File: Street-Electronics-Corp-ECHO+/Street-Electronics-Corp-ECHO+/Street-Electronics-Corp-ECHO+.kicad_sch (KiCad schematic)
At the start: 57 parts, among them J1 Bus_Apple_II_Card_Side, J2 STEREO, J3 MONO, U1 LM386, U10 74C74, U11 74LS02, U12 74LS02, U13 74LS02, U14 74LS02, U15 74LS00, U2 LM386, U3 TL084, U4 AY-3-8913, U5 AY-3-8913, U6 6522, U7 TMS5220, U8 74LS373, U9 74SC373

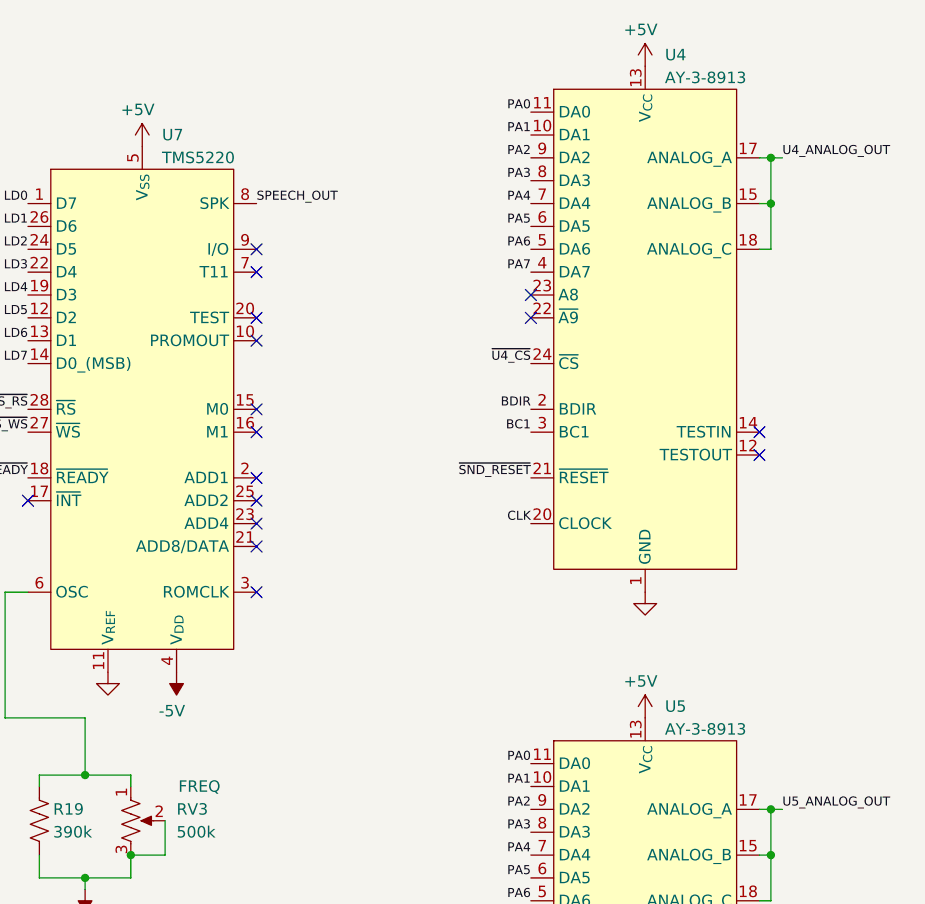
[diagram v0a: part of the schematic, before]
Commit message: Move the TMS sound chip into a shared Kicad lib
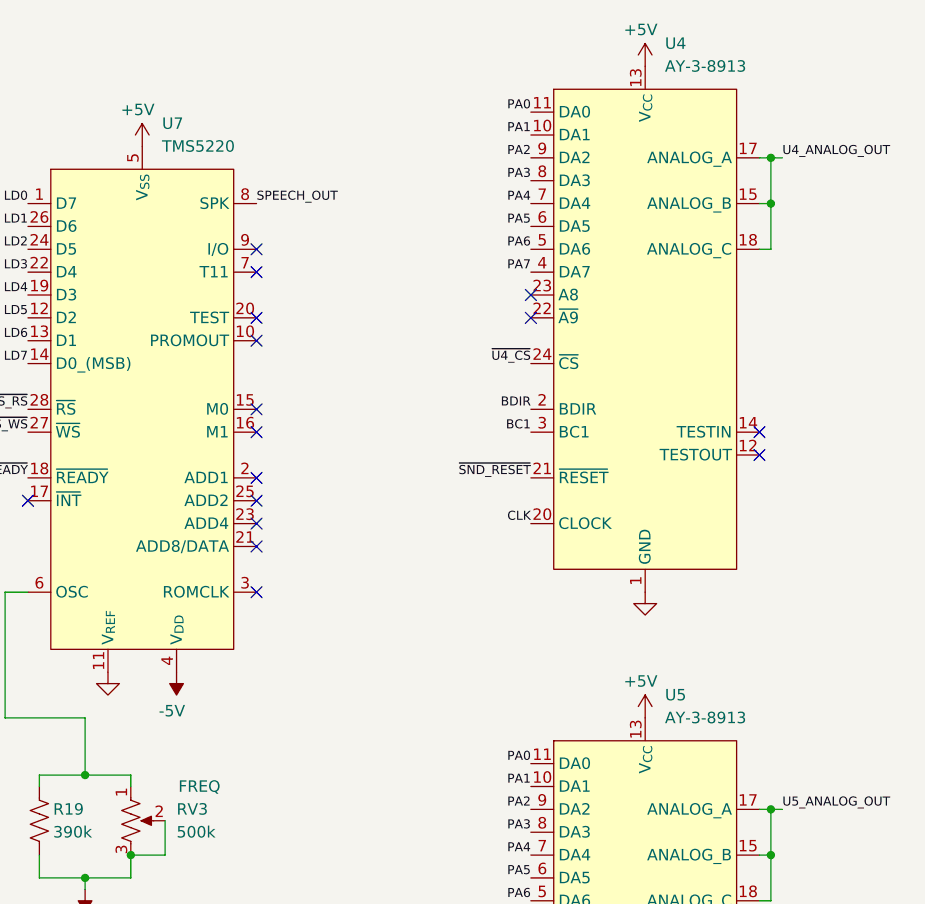
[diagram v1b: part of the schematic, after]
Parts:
- U4, U5: symbol Sound:AY-3-8913 -> Sound_Legacy:AY-3-8913
- U7: symbol Sound:TMS5220 -> Sound_Legacy:TMS5220
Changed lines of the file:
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@@
 	)
 	(symbol
-		(lib_id "Sound:AY-3-8913")
+		(lib_id "Sound_Legacy:AY-3-8913")
 		(at 381 52.07 0)
 		(unit 1)
@@
 		(fields_autoplaced yes)
 		(property "Reference" "U4"
-			(at 383.1941 21.59 0)
+			(at 383.1941 20.32 0)
 			(effects
 				(font
@@
 		)
 		(property "Value" "AY-3-8913"
-			(at 383.1941 24.13 0)
+			(at 383.1941 22.86 0)
 			(effects
 				(font
@@
 	)
 	(symbol
-		(lib_id "Sound:AY-3-8913")
+		(lib_id "Sound_Legacy:AY-3-8913")
 		(at 381 124.46 0)
 		(unit 1)
@@
 		(fields_autoplaced yes)
 		(property "Reference" "U5"
-			(at 383.1941 93.98 0)
+			(at 383.1941 92.71 0)
 			(effects
 				(font
@@
 		)
 		(property "Value" "AY-3-8913"
-			(at 383.1941 96.52 0)
+			(at 383.1941 95.25 0)
 			(effects
 				(font
@@
 	)
 	(symbol
-		(lib_id "Sound:TMS5220")
+		(lib_id "Sound_Legacy:TMS5220")
 		(at 325.12 60.96 0)
 		(unit 1)
@@
 		(fields_autoplaced yes)
 		(property "Reference" "U7"
-			(at 327.3141 30.48 0)
+			(at 327.3141 29.21 0)
 			(effects
 				(font
@@
 		)
 		(property "Value" "TMS5220"
-			(at 327.3141 33.02 0)
+			(at 327.3141 31.75 0)
 			(effects
 				(font
